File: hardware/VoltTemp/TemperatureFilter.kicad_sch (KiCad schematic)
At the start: 9 parts, among them U4 TLV9062xD

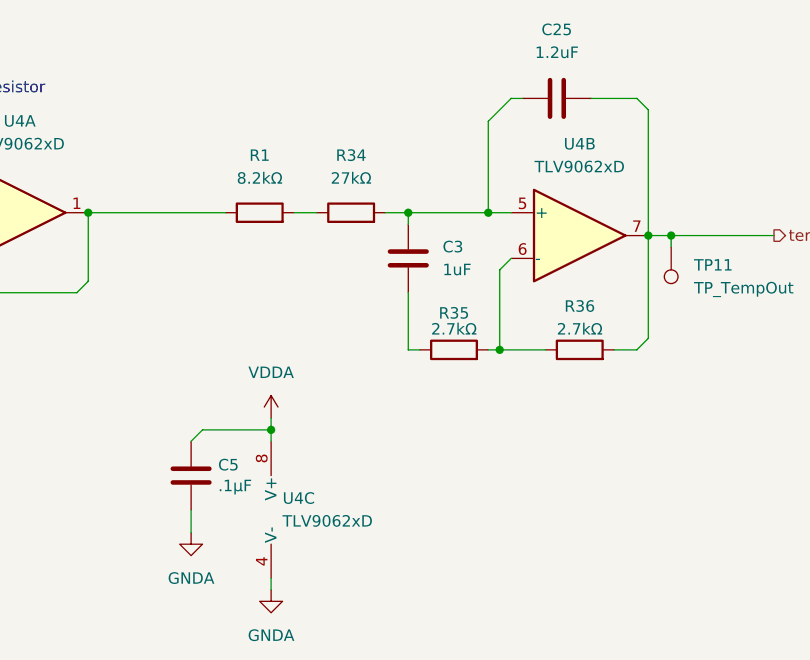
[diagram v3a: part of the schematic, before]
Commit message: Bom (#3)
* bom

* bom for cell sim and thermistor

* stopped displaying part numbers in schematic
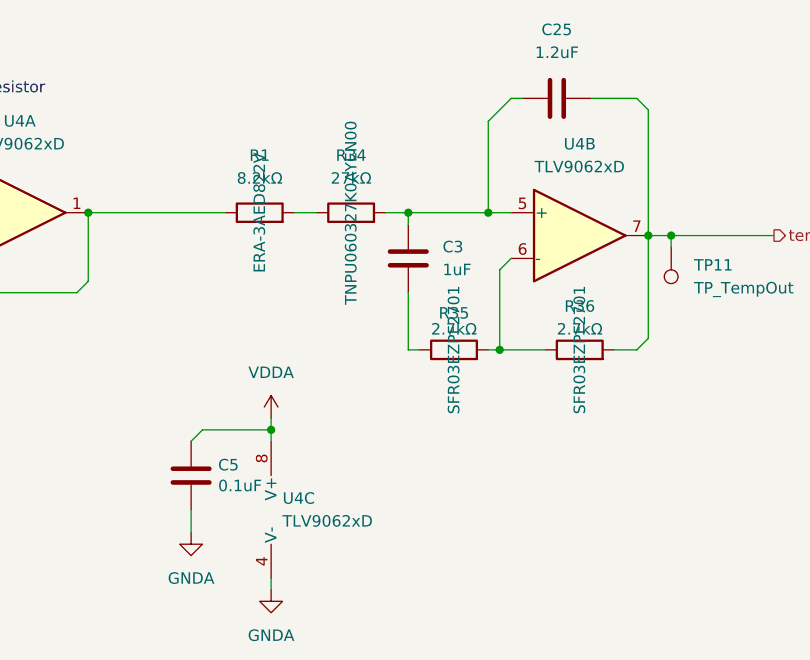
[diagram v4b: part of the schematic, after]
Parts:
- C25: P/N (none) -> C0805C125K4RACTU
- C5: value .1μF -> 0.1uF
- R1: P/N (none) -> ERA-3AED822V
- R34: P/N (none) -> TNPU060327K0AYEN00
- R35, R36: P/N (none) -> SFR03EZPF2701
- U4: P/N (none) -> TLV9062QDGKRQ1
